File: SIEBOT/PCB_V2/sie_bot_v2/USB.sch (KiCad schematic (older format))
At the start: 38 parts, among them J3 USB_2A, J4 USB_2A, U4 GL850G, U5 RCLAMP0502B, U6 RCLAMP0502B, U7 RCLAMP0502B, U8 RCLAMP0502B, U9 MCP130, X2 12MHz

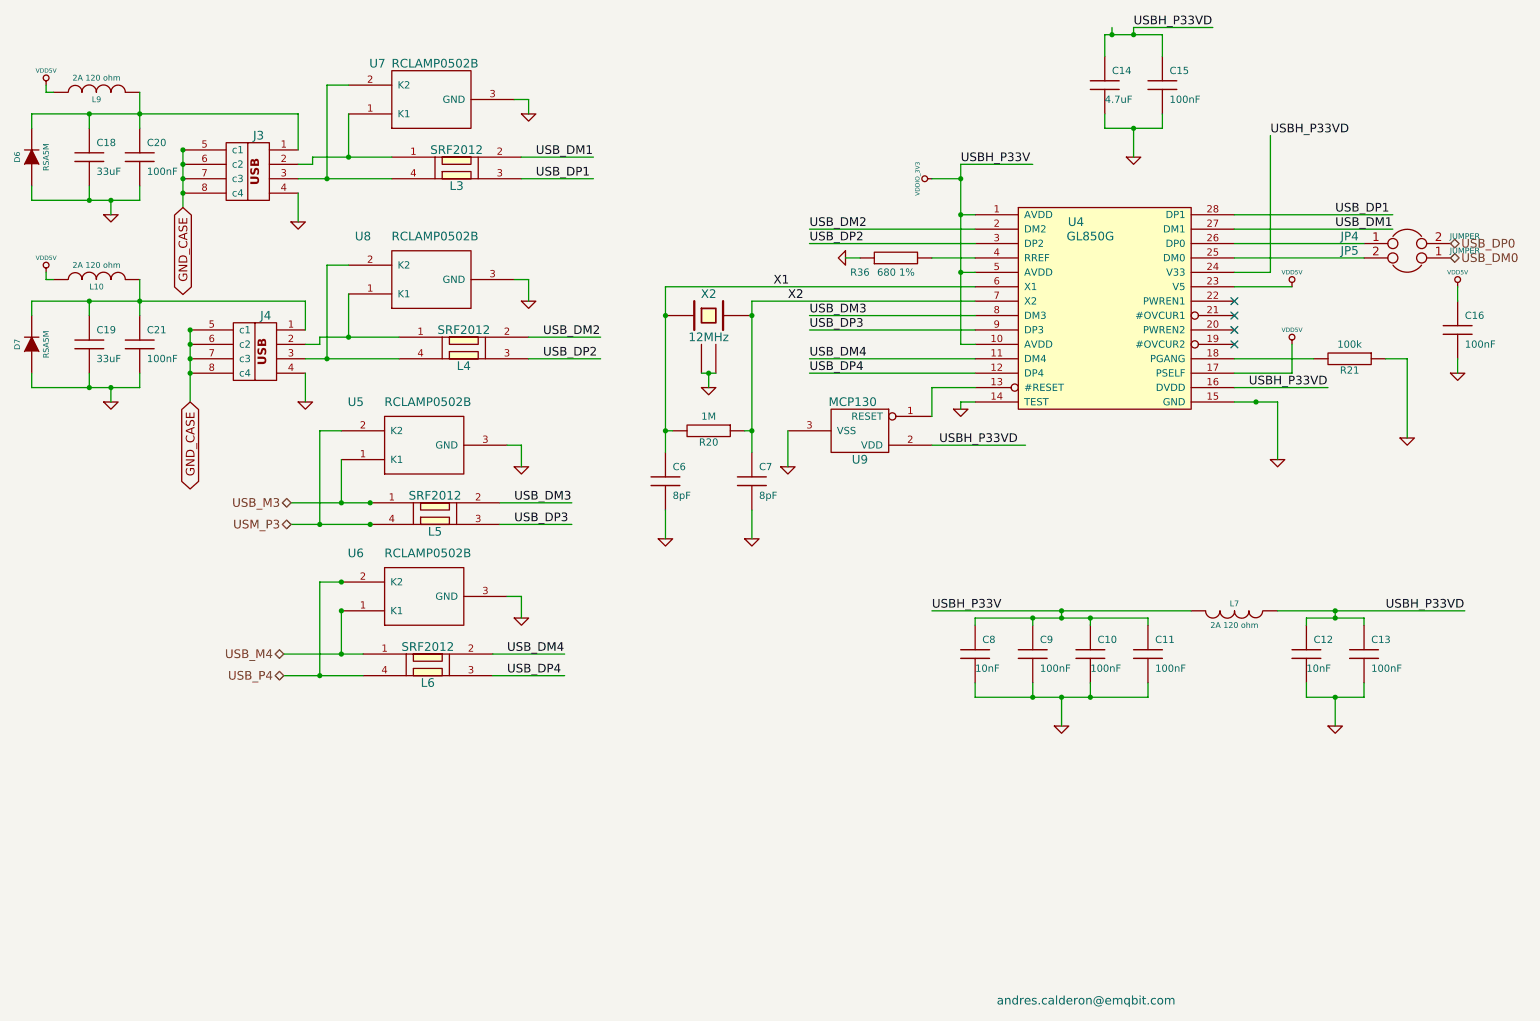
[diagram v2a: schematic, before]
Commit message: Ruteo de la conexión entre el procesador y el STM32, re-localización de los conectores de alimentación y USB, adidición del regulador de 3.3V
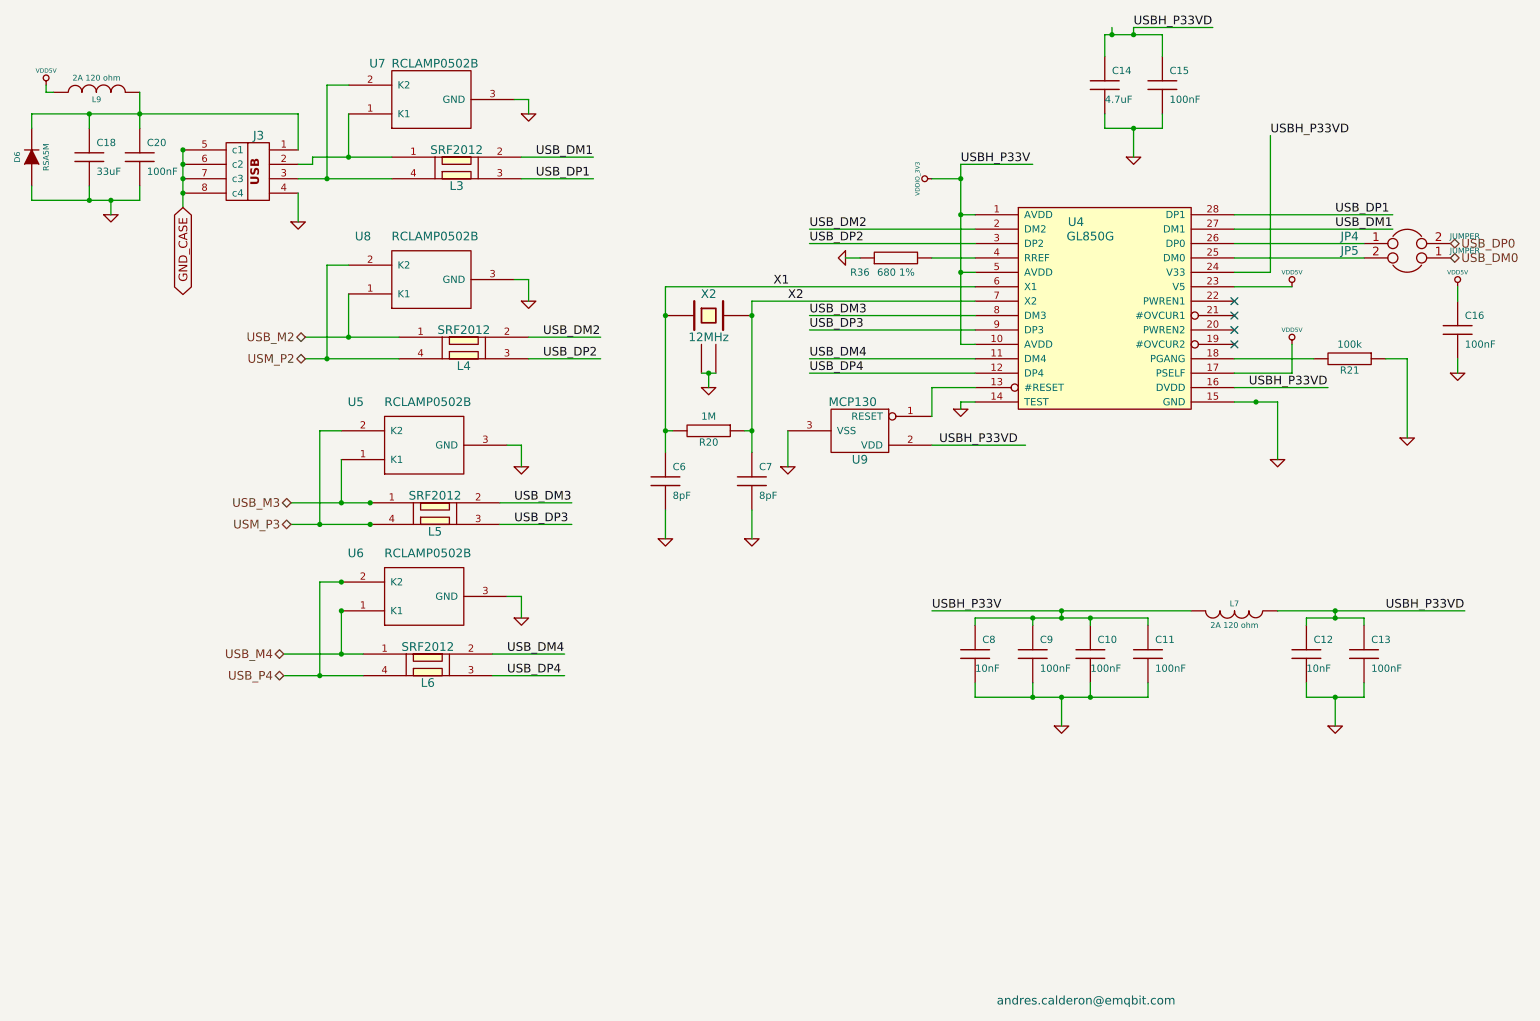
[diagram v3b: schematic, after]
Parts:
- removed C19: 33uF, SM1206, symbol C
- removed C21: 100nF, SM0603, symbol C
- removed D7: RSA5M, diode-1-SOD123, symbol DIODE
- removed J4: USB_2A, symbol USB_2A
- removed L10: 2A 120 ohm, SM0805, symbol INDUCTOR
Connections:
- net labels added: USB_M2, USM_P2
- wire segments 147 -> 131
